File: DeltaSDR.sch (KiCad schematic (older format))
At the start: 57 parts, among them J1 Conn_01x03_Male, J2 Conn_01x05_Male, J3 Barrel_Jack, J4 USB_A, J6 Conn_01x02_Male, Q7 MMBT3904, U1 TC1262-33, U2 Si570, U4 PCM3060, U5 CY8C3246PVI-147, U6 TC1262-5, U7 TC1262-5, U8 74HC74, Y1 Crystal_GND24

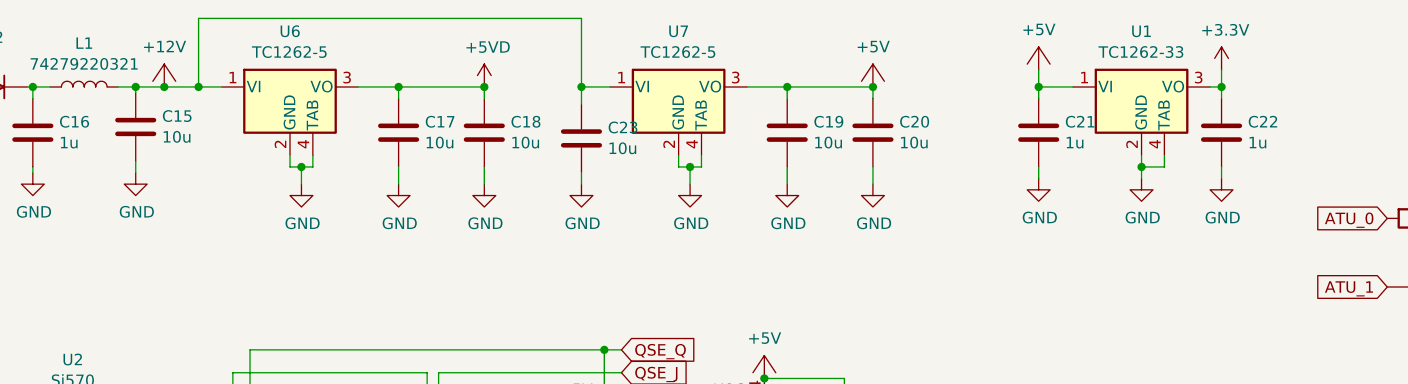
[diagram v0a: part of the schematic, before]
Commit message: Changed LDOs
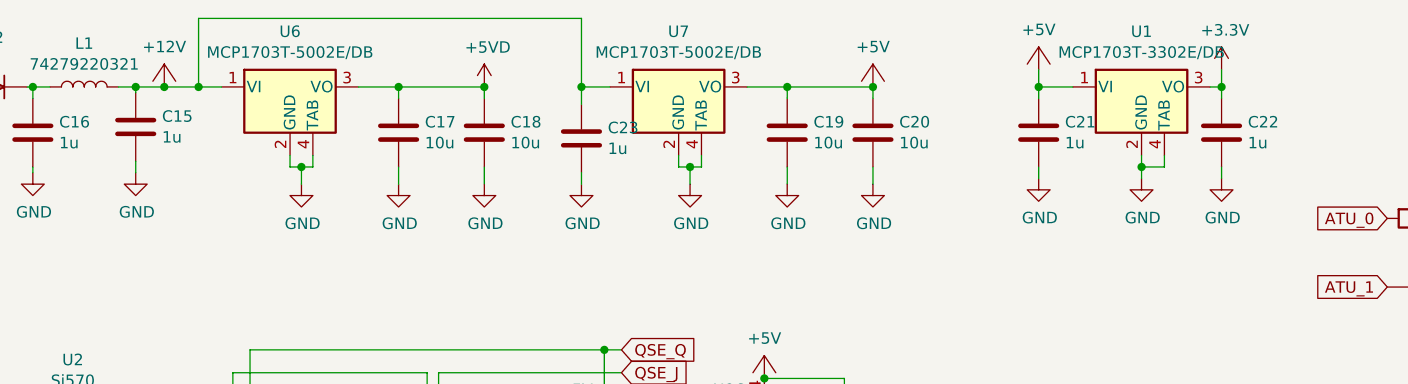
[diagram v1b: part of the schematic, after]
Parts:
- C15, C23: value 10u -> 1u
- U1: value TC1262-33 -> MCP1703T-3302E/DB
- U6, U7: value TC1262-5 -> MCP1703T-5002E/DB
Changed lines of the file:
@@
 EESchema Schematic File Version 4
-LIBS:DeltaSDR-cache
-EELAYER 29 0
+EELAYER 30 0
 EELAYER END
 $Descr A4 11693 8268
@@
 P 6675 950
 F 0 "U1" H 6675 1192 50  0000 C CNN
-F 1 "TC1262-33" H 6675 1101 50  0000 C CNN
+F 1 "MCP1703T-3302E/DB" H 6675 1101 50  0000 C CNN
 F 2 "Package_TO_SOT_SMD:SOT-223" H 6675 1175 50  0001 C CIN
-F 3 "http://ww1.microchip.com/downloads/en/DeviceDoc/21373C.pdf" H 6675 650 50  0001 C CNN
+F 3 "" H 6675 650 50  0001 C CNN
 	1    6675 950
 	1    0    0    -1
@@
 P 2275 1125
 F 0 "C15" H 2390 1171 50  0000 L CNN
-F 1 "10u" H 2390 1080 50  0000 L CNN
+F 1 "1u" H 2390 1080 50  0000 L CNN
 F 2 "Capacitor_SMD:C_0805_2012Metric" H 2313 975 50  0001 C CNN
 F 3 "~" H 2275 1125 50  0001 C CNN
@@
 P 4225 1175
 F 0 "C23" H 4340 1221 50  0000 L CNN
-F 1 "10u" H 4340 1130 50  0000 L CNN
+F 1 "1u" H 4340 1130 50  0000 L CNN
 F 2 "Capacitor_SMD:C_0805_2012Metric" H 4263 1025 50  0001 C CNN
 F 3 "~" H 4225 1175 50  0001 C CNN
@@
 P 2950 950
 F 0 "U6" H 2950 1192 50  0000 C CNN
-F 1 "TC1262-5" H 2950 1101 50  0000 C CNN
+F 1 "MCP1703T-5002E/DB" H 2950 1101 50  0000 C CNN
 F 2 "Package_TO_SOT_SMD:SOT-223" H 2950 1175 50  0001 C CIN
 F 3 "http://ww1.microchip.com/downloads/en/DeviceDoc/21373C.pdf" H 2950 650 50  0001 C CNN
@@
 P 4650 950
 F 0 "U7" H 4650 1192 50  0000 C CNN
-F 1 "TC1262-5" H 4650 1101 50  0000 C CNN
+F 1 "MCP1703T-5002E/DB" H 4650 1101 50  0000 C CNN
 F 2 "Package_TO_SOT_SMD:SOT-223" H 4650 1175 50  0001 C CIN
 F 3 "http://ww1.microchip.com/downloads/en/DeviceDoc/21373C.pdf" H 4650 650 50  0001 C CNN
